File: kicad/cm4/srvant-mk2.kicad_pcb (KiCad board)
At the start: 6 copper layers, 80 x 100 mm, 83 parts, among them J1 Screw_Terminal_01x02, J10 HDMI connector, J14 JST_SHBM04B-SRSS-TB, J2 USB_B_Micro, J5 Conn_01x03, J6 Conn_01x03, J7 ARJM11, J8 Bus_M.2_Socket_M, J9 Conn_02x10_Odd_Even, U1 INA219AxDCN, U10 ASEK-32.768KHZ-L-R-T, U4 TPD4EUSB30, U5 TPD4EUSB30, U6 SLB9670VQ20FW785XTMA1, U8 74LVC1G07SE-7, U9 RT9742SNGV

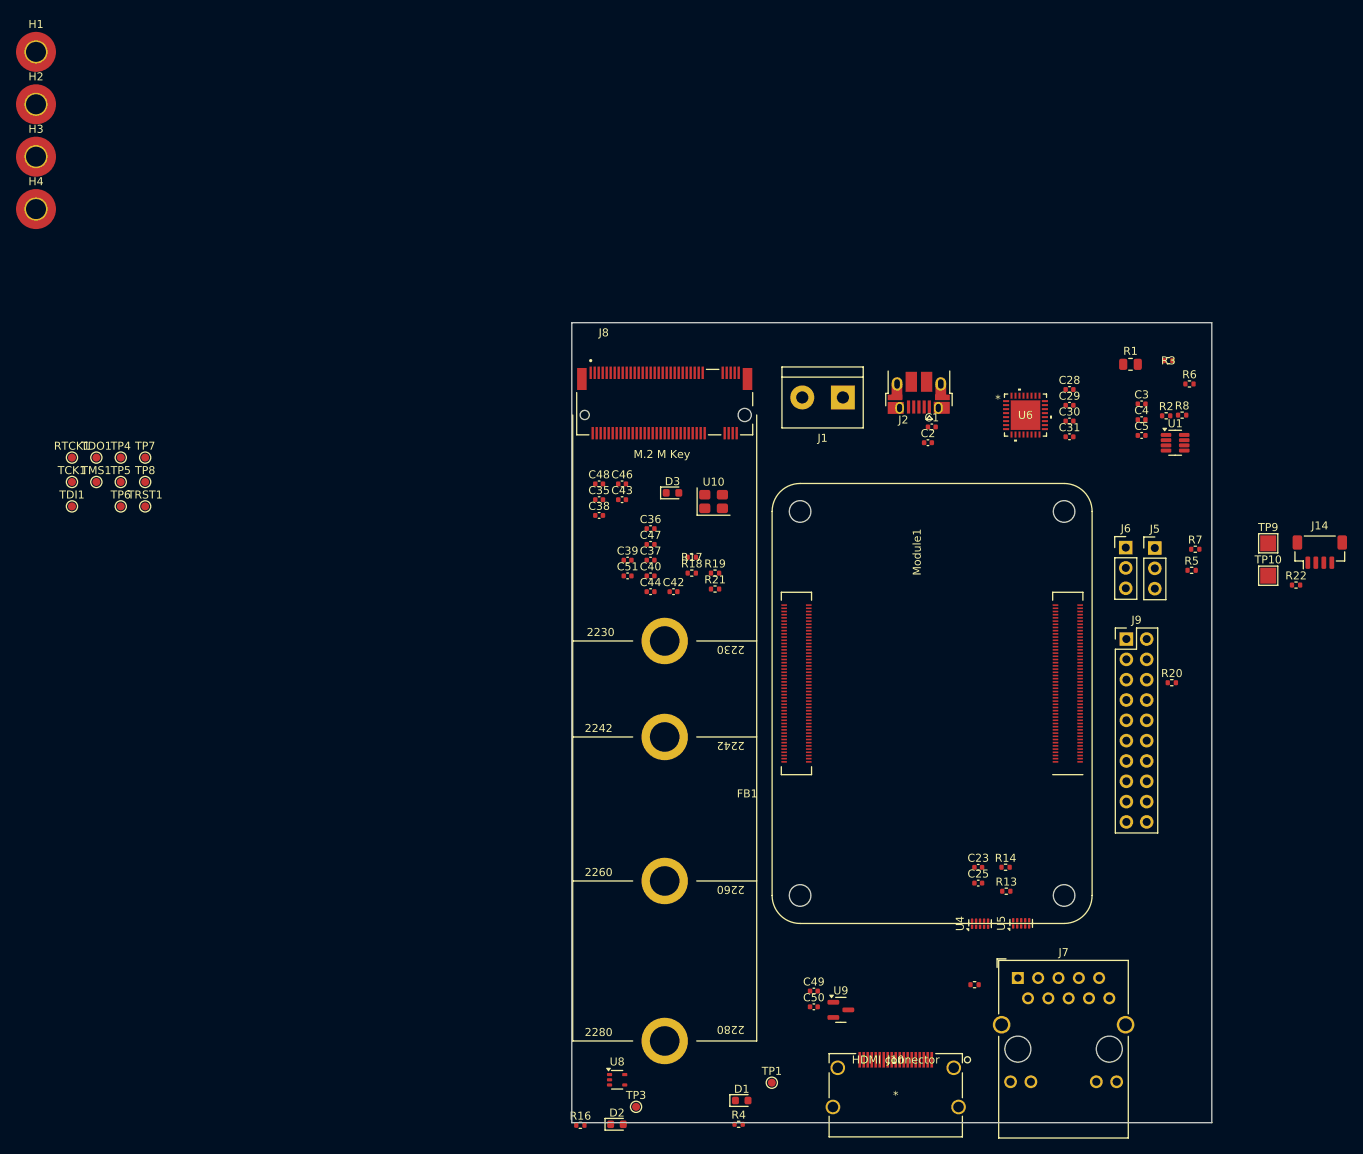
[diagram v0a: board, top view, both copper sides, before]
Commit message: state of the cm4(5), manufactured revision
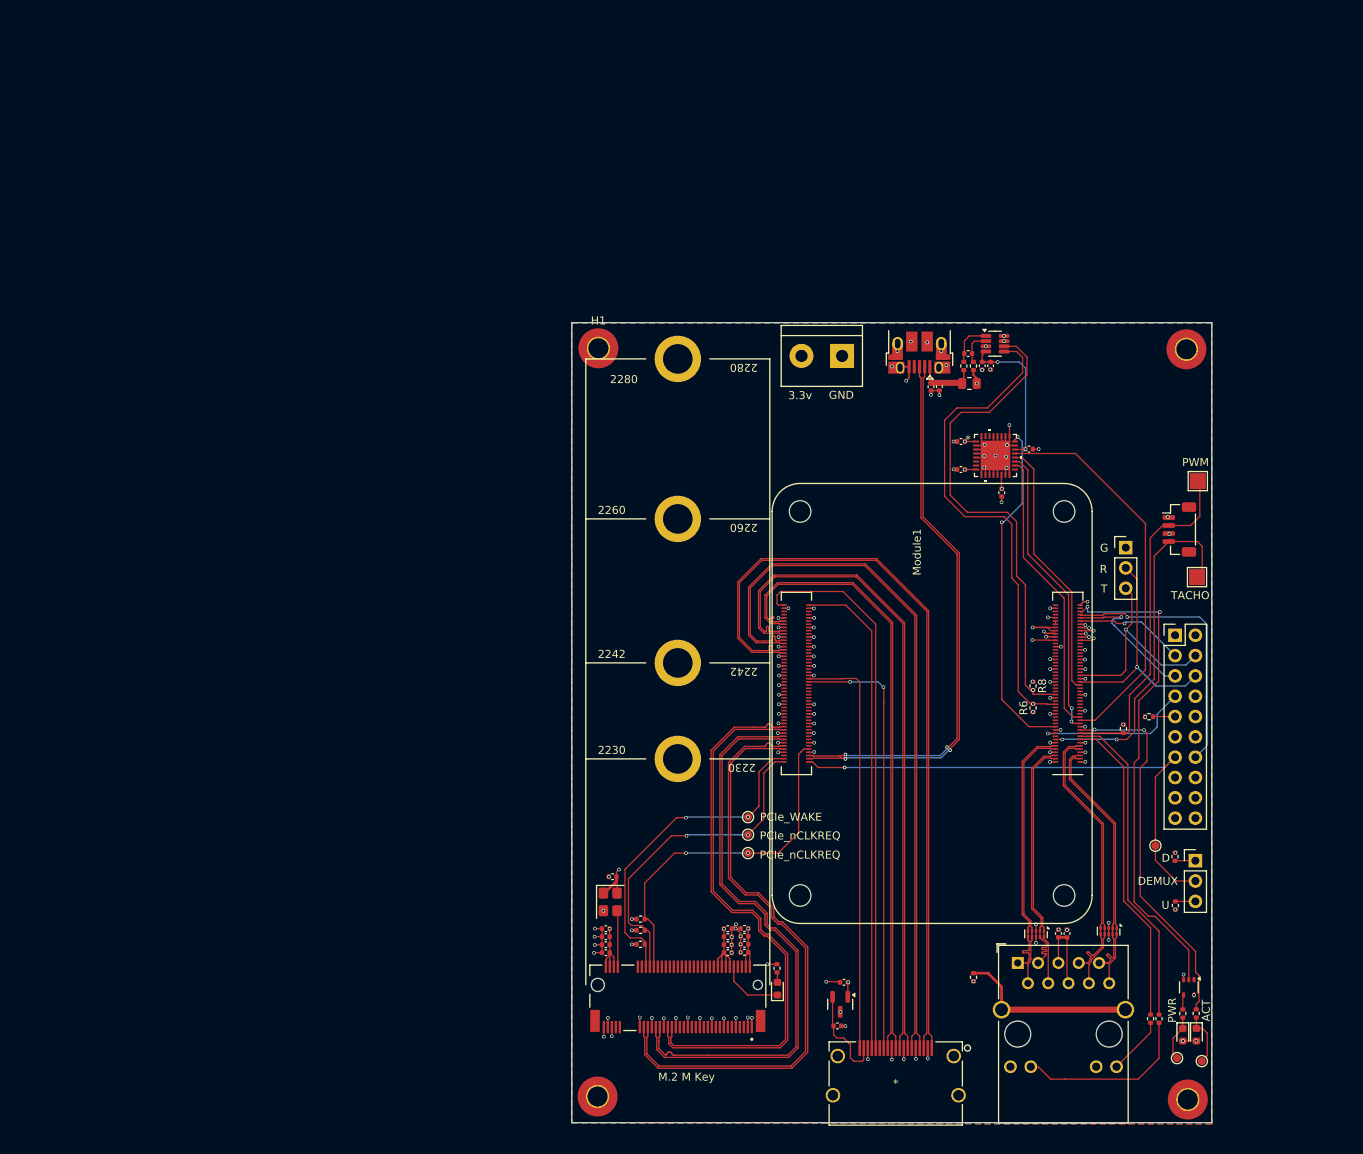
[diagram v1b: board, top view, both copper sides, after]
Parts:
- removed RTCK1: RTCK, TestPoint:TestPoint_Pad_D1.0mm
- removed TCK1: TCK, TestPoint:TestPoint_Pad_D1.0mm
- removed TDI1: TDI, TestPoint:TestPoint_Pad_D1.0mm
- removed TDO1: TDO, TestPoint:TestPoint_Pad_D1.0mm
- removed TMS1: TMS, TestPoint:TestPoint_Pad_D1.0mm
- removed TP6, TP7: PCIe_nRST, TestPoint:TestPoint_Pad_D1.0mm
- removed TRST1: TRST, TestPoint:TestPoint_Pad_D1.0mm
- added TP11: PCIe_nCLKREQ, TestPoint:TestPoint_Pad_D1.0mm, F.Cu at (127.0, 121.8)
- moved H2 190.3 mm to (182.0, 157.1)
- moved H3 145.8 mm to (181.8, 63.3)
- moved TP8 134.2 mm to (177.9, 125.4)
- moved H4 131.3 mm to (108.2, 156.7)
- moved TP4 92.7 mm to (127.0, 126.3)
- moved TP5 90.0 mm to (127.0, 124.0)
- moved H1 79.5 mm to (108.3, 63.2)
- moved R16 76.6 mm to (181.4, 146.3), turned to 90 degrees
- moved U8 72.4 mm to (182.1, 143.1), turned to -90 degrees
- moved D2 71.6 mm to (181.4, 149.0), turned to -90 degrees
- moved J8 71.3 mm to (118.2, 142.8), turned to 180 degrees
- moved TP3 67.9 mm to (180.7, 151.9)
- moved D3 63.3 mm to (130.7, 143.2), turned to 90 degrees
- moved C48 60.8 mm to (124.5, 138.8)
- moved R4 58.8 mm to (183.1, 146.3), turned to 90 degrees
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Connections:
- C1 pad 1: /+5v_HOST -> /+5v_IN
- C2 pad 1: /+5v_HOST -> /+5v_IN
- C4 pad 1: /+3v3 (BMC) -> /+3.3v_HOST
- C5 pad 1: /+3v3 (BMC) -> /+3.3v_HOST
- J2 pad 1: /+5v_HOST -> /+5v_IN
- Module1 pad 100: /CAM_GPIO1 -> unconnected-(Module1A-CAM_GPIO1-Pad100)
- Module1 pad 102: /PCIE_nCLKREQ -> /PCIE_CLK_nREQ
- Module1 pad 104: /PCIE_nWAKE -> /PCIE_WAKE
- Module1 pad 153: unconnected-(Module1B-HDMI0_HOTPLUG-Pad153) -> /HDMI0_HOTPLUG
- Module1 pad 94: /CC1 -> unconnected-(Module1A-CC1-Pad94)
- Module1 pad 96: /CC2 -> unconnected-(Module1A-CC2-Pad96)
- R1 pad 1: /SENSE_IN- -> /+5v_HOST
- R1 pad 2: /+5v_HOST -> /+5v_IN
- R2 pad 1: /+5v_HOST -> /+5v_IN
- R3 pad 1: /SENSE_IN- -> /+5v_HOST
- R5 pad 1: Net-(J5-Pin_1) -> Net-(J5-Pin_3)
- R6 pad 1: /+3v3 (BMC) -> /+3.3v_HOST
- R7 pad 2: Net-(J5-Pin_3) -> Net-(J5-Pin_1)
- R8 pad 1: /+3v3 (BMC) -> /+3.3v_HOST
- U1 pad 4: /+3v3 (BMC) -> /+3.3v_HOST
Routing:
- net GND: track 0.00 -> 131.7 mm, vias 0 -> 123
- net /GPIO10: track 0.00 -> 97.3 mm, vias 0 -> 1
- net /HDMI0_D2_P: track 0.00 -> 96.2 mm
- net /HDMI0_D2_N: track 0.00 -> 96.2 mm
- net /GPIO11: track 0.00 -> 94.1 mm, vias 0 -> 1
- net /HDMI0_D1_P: track 0.00 -> 90.0 mm
- net /HDMI0_D1_N: track 0.00 -> 90.0 mm
- net /HDMI0_D0_P: track 0.00 -> 83.0 mm
- net /HDMI0_D0_N: track 0.00 -> 83.0 mm
- net /HDMI0_CK_P: track 0.00 -> 77.6 mm
- net /HDMI0_CK_N: track 0.00 -> 77.6 mm
- net /PCIE_CLK_P: track 0.00 -> 74.2 mm
- net /PCIE_CLK_N: track 0.00 -> 74.1 mm
- net /PCIE_RX_P: track 0.00 -> 72.0 mm
- net /PCIE_RX_N: track 0.00 -> 72.0 mm
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- added copper zone on In3.Cu, net /+3.3v_HOST
- added copper zone on In3.Cu, net /+3v3_AUX
- added copper zone on In3.Cu, net /+5v_HOST
- added copper zone on B.Cu, net GND
- added copper zone on F.Cu, net GND
- added copper zone on In1.Cu, net GND
- added copper zone on In2.Cu, net GND
- added copper zone on In4.Cu, net GND
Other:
- board text added: "3.3v"
- board text added: "ACT"
- board text added: "D"
- board text added: "DEMUX"
- board text added: "G"
- board text added: "GND"
- board text added: "PCIe_WAKE"
- board text added: "PCIe_nCLKREQ"
- board text added: "PWM"
- board text added: "PWR"
- board text added: "R"
- board text added: "T"
- board text added: "TACHO"
- board text added: "U"
